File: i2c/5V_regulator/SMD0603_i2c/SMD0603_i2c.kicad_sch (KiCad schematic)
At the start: 22 parts, among them J1 Conn_01x04, J2 Conn_01x04, Q1 MMBT5551L, Q2 BSS138, Q3 BSS138, U1 TPS61222DCK, U2 LMV321, U3 MCP4725xxx-xCH

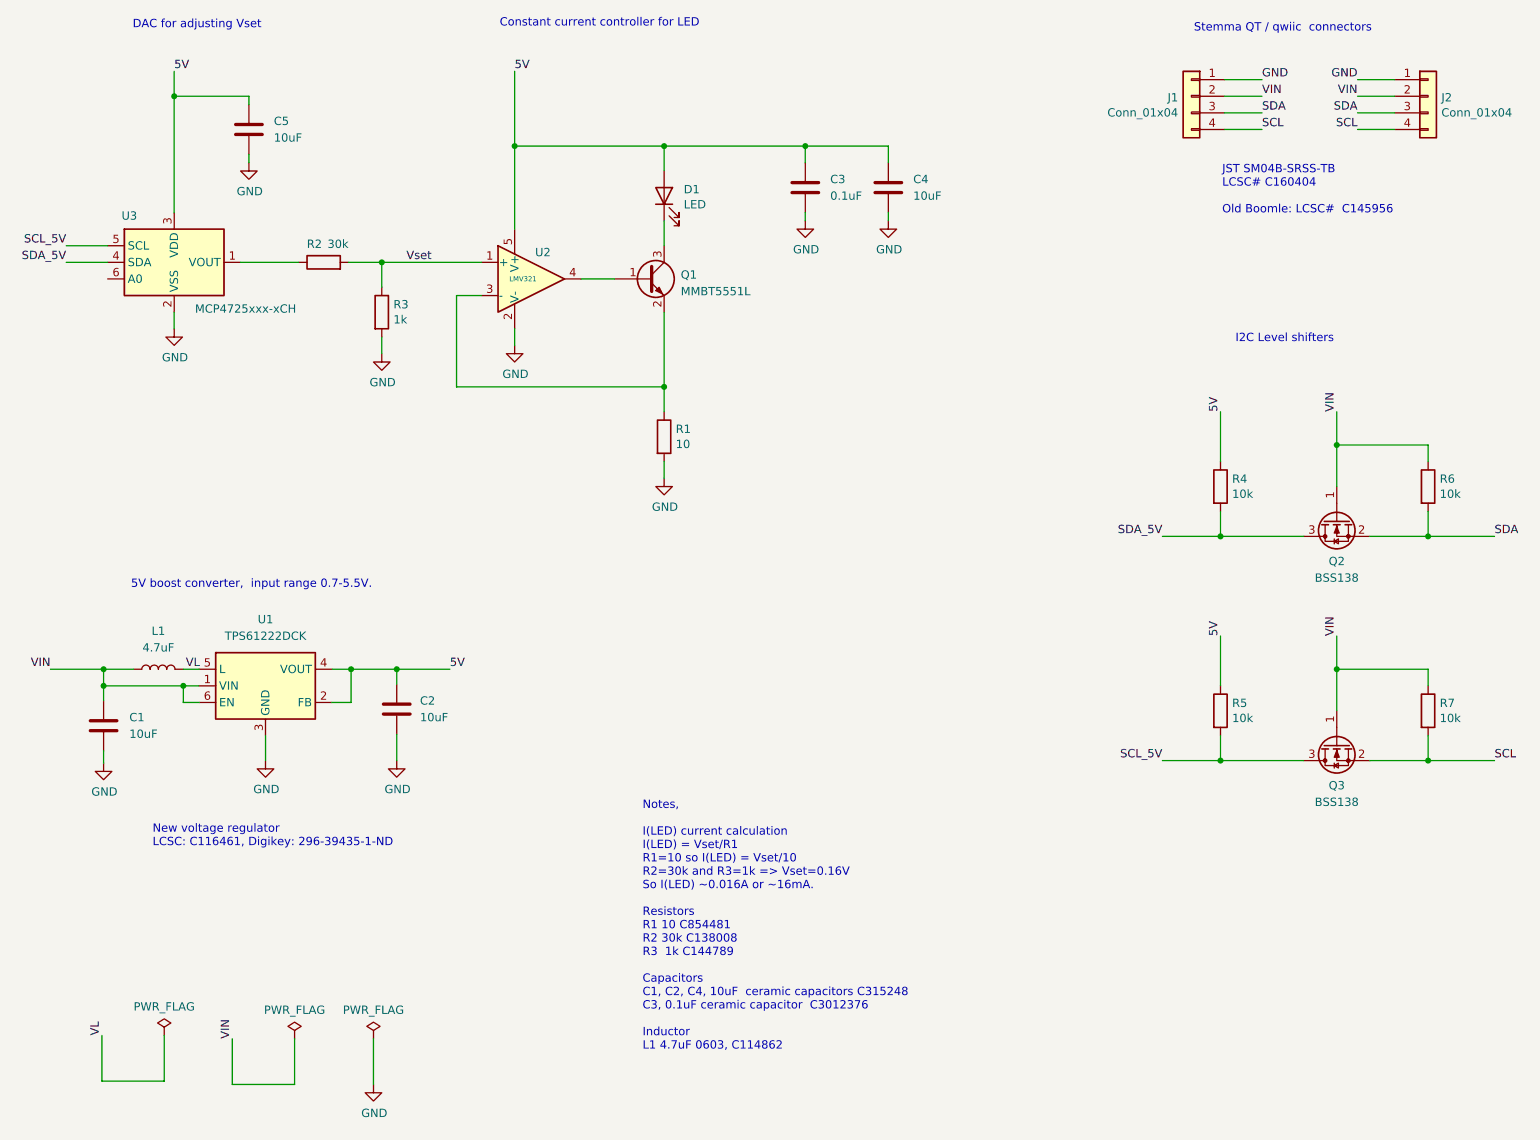
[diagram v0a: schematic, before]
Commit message: Worked on I2C current controlled LED board.
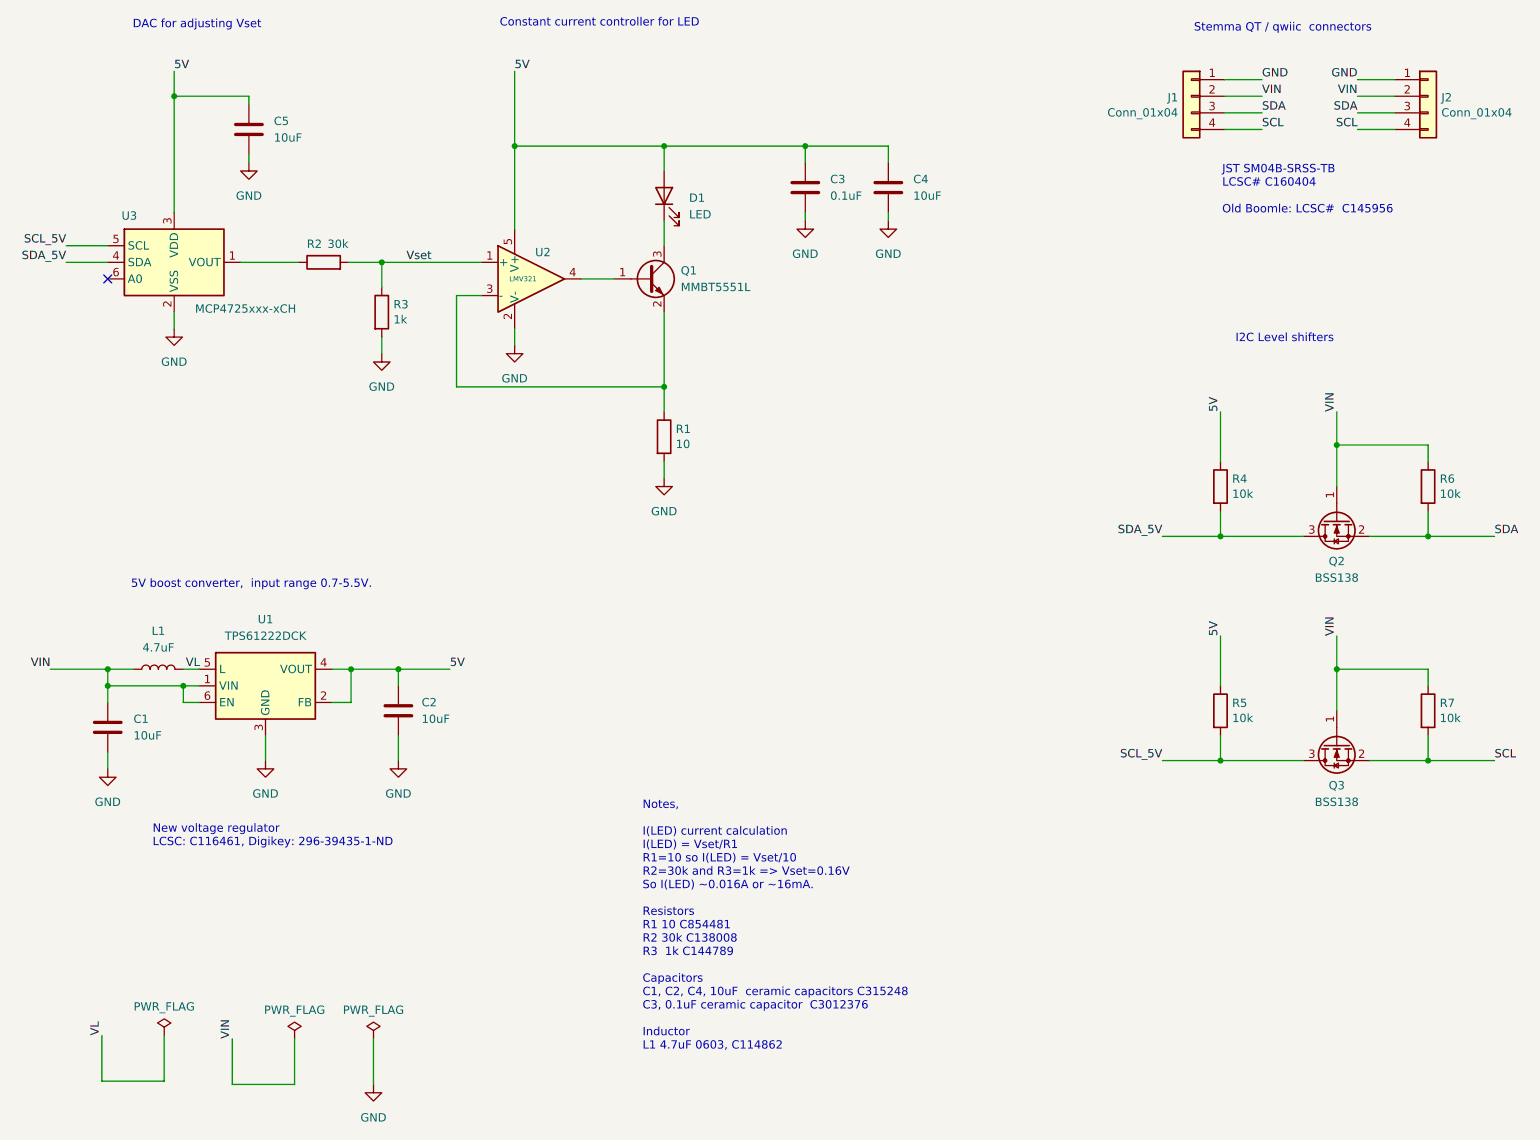
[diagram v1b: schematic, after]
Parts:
- D1: footprint LED_SMD:LED_0603_1608Metric -> (none)
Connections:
- no-connect marks 0 -> 1
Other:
- moved on the sheet: C1

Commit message: Worked on layout and routing for 5V i2c controlled design.
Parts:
- added C6: 10uF, Capacitor_SMD:C_0805_2012Metric, symbol Device:C
- C1, C4, C5: footprint Capacitor_SMD:C_0402_1005Metric -> Capacitor_SMD:C_0603_1608Metric; LCSC Part # (none) -> C962136
- C2: footprint Capacitor_SMD:C_0402_1005Metric -> Capacitor_SMD:C_0805_2012Metric; LCSC Part # (none) -> C1713
- C3: LCSC Part # (none) -> C1525
- D1: footprint (none) -> LED_SMD:LED_0603_1608Metric
- J1, J2: LCSC Part # (none) -> C160404
- L1: LCSC Part # (none) -> C114862
- Q1: LCSC Part # (none) -> C41095
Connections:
- net 5V: now also C6.2
- net GND: now also C6.1
